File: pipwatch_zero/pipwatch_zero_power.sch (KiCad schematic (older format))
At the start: 18 parts, among them U201 MICRO-B_USB, U202 USB6BX, U203 MCP73831, U204 LD59015C33R

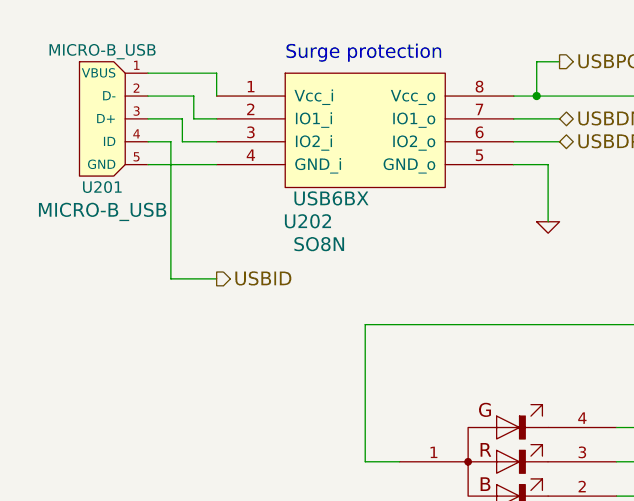
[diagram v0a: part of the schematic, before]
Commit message: pipwatch_zero layout complete
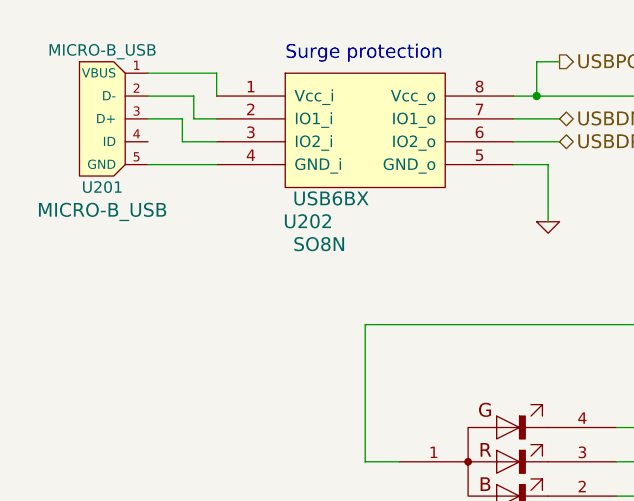
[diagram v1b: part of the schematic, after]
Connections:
- net USBID: no longer names the net of U201.4 (ID)
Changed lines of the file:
@@
 Text Notes 8750 2950 0    60   ~ 0
 Low-Drop Regulator
-Text HLabel 1800 3900 2    60   Output ~ 0
-USBID
-Wire Wire Line
-	1500 3300 1600 3300
-Wire Wire Line
-	1600 3300 1600 3900
-Wire Wire Line
-	1600 3900 1800 3900
 $EndSCHEMATC

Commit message: pipwatch_zero hw02, sent to pragoboard
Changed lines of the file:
@@
 encoding utf-8
 Sheet 2 5
-Title ""
-Date "31 aug 2014"
-Rev ""
+Title "PIPWATCH ZERO"
+Date "3 sep 2014"
+Rev "HW02"
 Comp ""
 Comment1 ""
@@
 F 0 "BAT201" H 6900 3900 50  0000 C CNN
 F 1 "BL4C" H 6900 3800 50  0000 C CNN
-F 2 "do214aa" V 6850 3400 60  0001 C CNN
+F 2 "do214aa" V 6850 3400 60  0000 C CNN
 F 3 "" H 6700 3850 60  0000 C CNN
 	1    6700 3850
